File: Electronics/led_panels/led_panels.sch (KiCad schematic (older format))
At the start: 226 parts, among them P5 CONN_2, P6 CONN_2

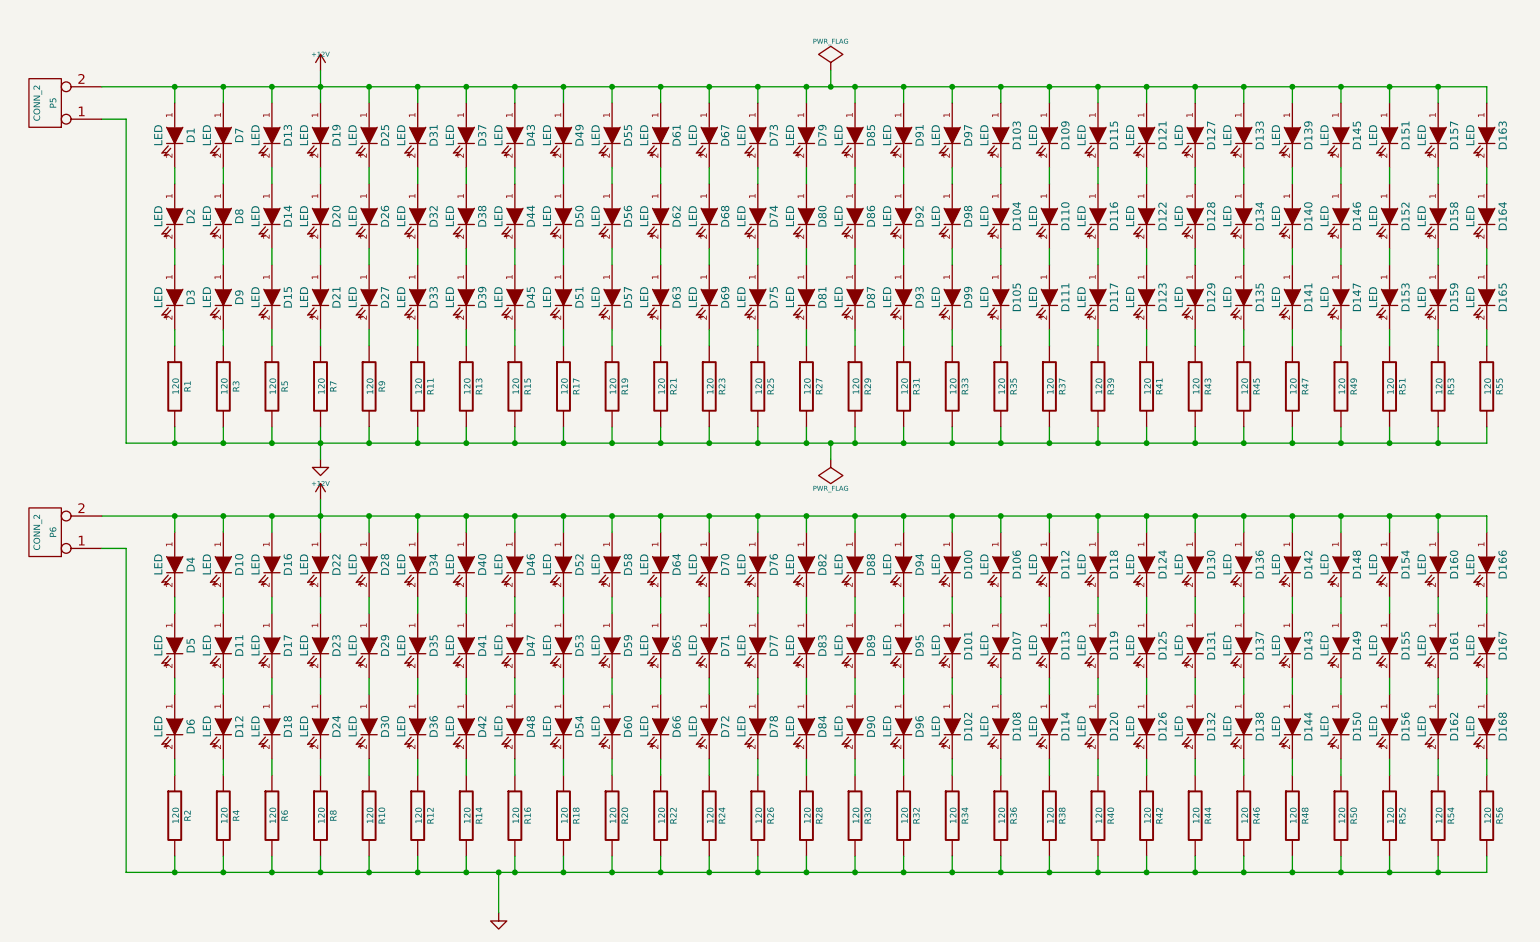
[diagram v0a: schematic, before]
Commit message: Updated board layout. Tidied up schematic.
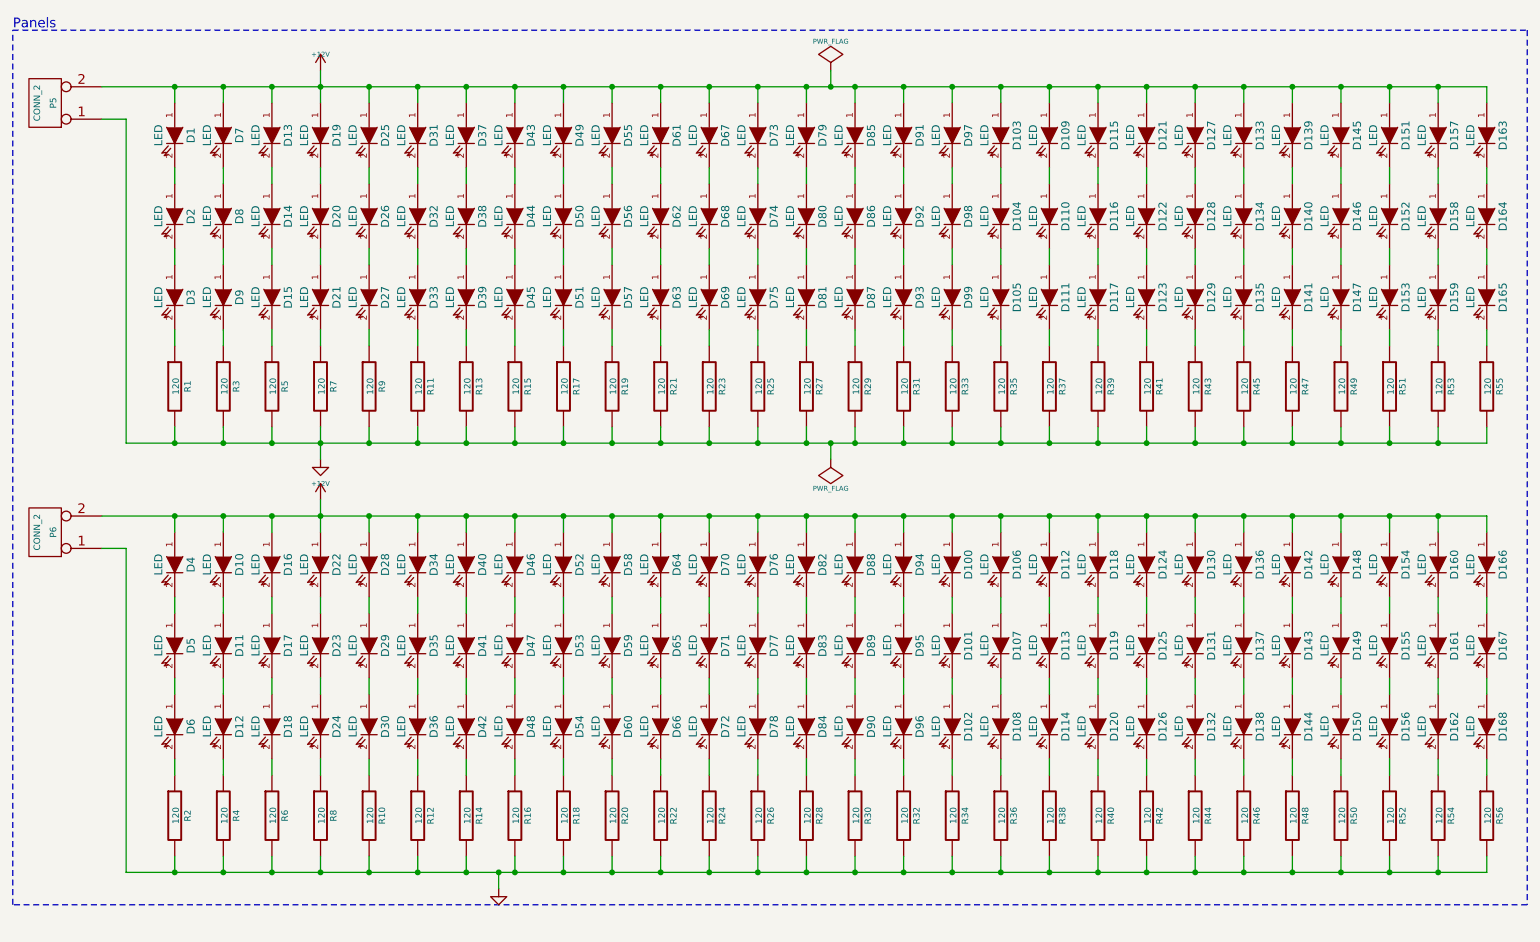
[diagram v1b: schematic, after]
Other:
- note added: "Panels"

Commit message: Tidying.
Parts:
- renumbered P5 to P1, P6 to P2
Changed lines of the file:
@@
 $EndComp
 $Comp
-L CONN_2 P5
+L CONN_2 P1
 U 1 1 5480B6EC
 P 1300 1150
-F 0 "P5" V 1250 1150 40  0000 C CNN
+F 0 "P1" V 1250 1150 40  0000 C CNN
 F 1 "CONN_2" V 1350 1150 40  0000 C CNN
 F 2 "Connect:bornier2" H 1300 1150 60  0001 C CNN
@@
 $EndComp
 $Comp
-L CONN_2 P6
+L CONN_2 P2
 U 1 1 5480BA09
 P 1300 3800
-F 0 "P6" V 1250 3800 40  0000 C CNN
+F 0 "P2" V 1250 3800 40  0000 C CNN
 F 1 "CONN_2" V 1350 3800 40  0000 C CNN
 F 2 "Connect:bornier2" H 1300 3800 60  0001 C CNN

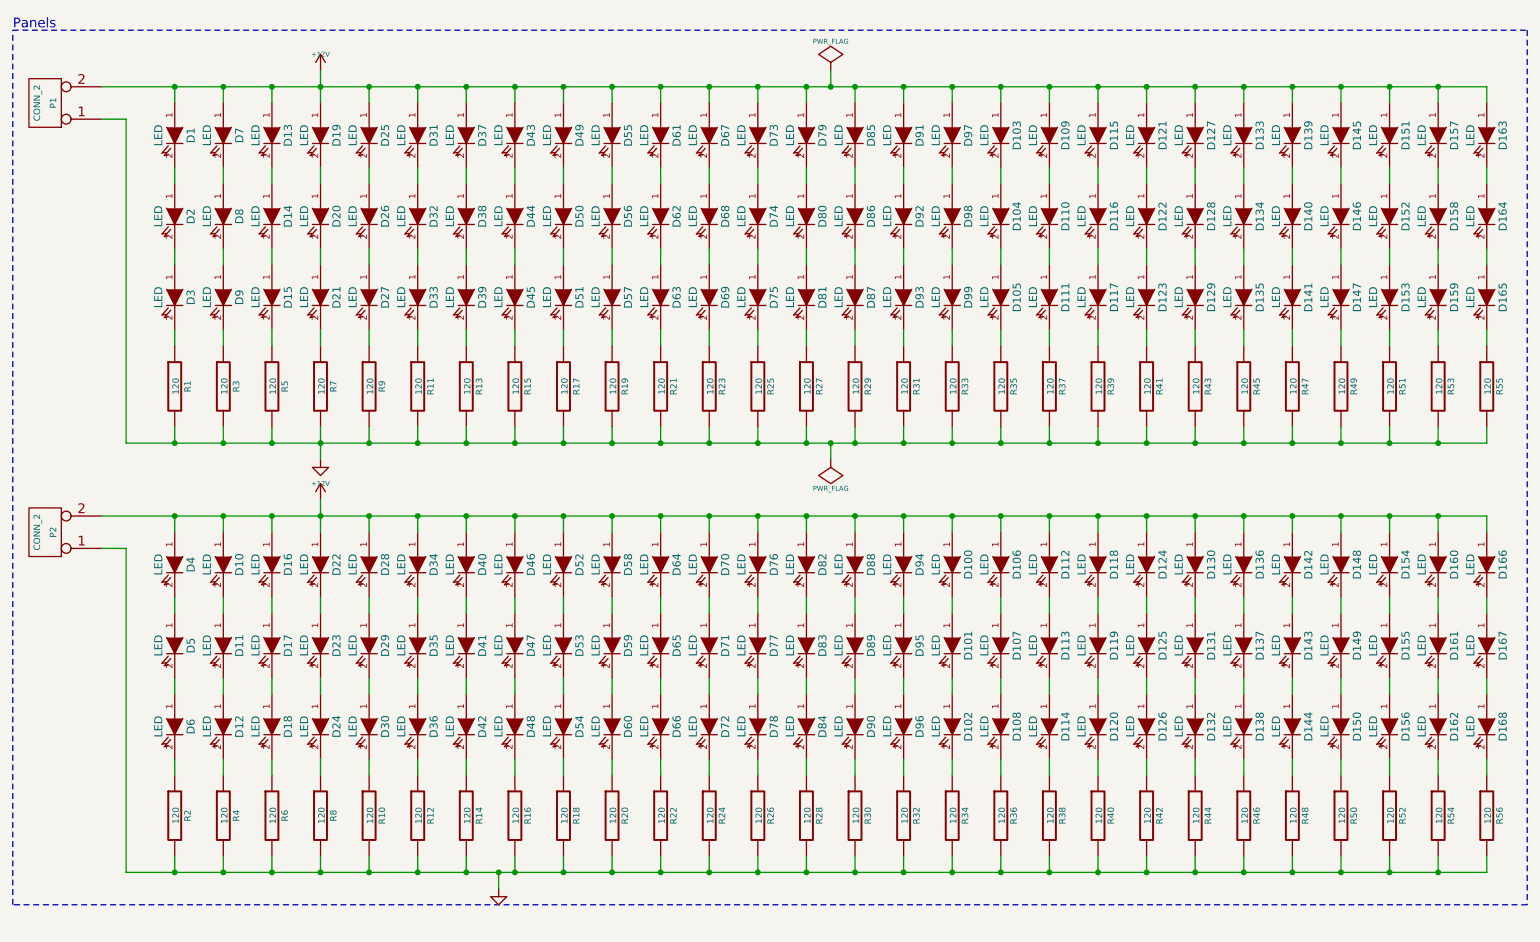
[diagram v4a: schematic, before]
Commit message: Trying out a PCB-based LED panel instead of Veroboard.
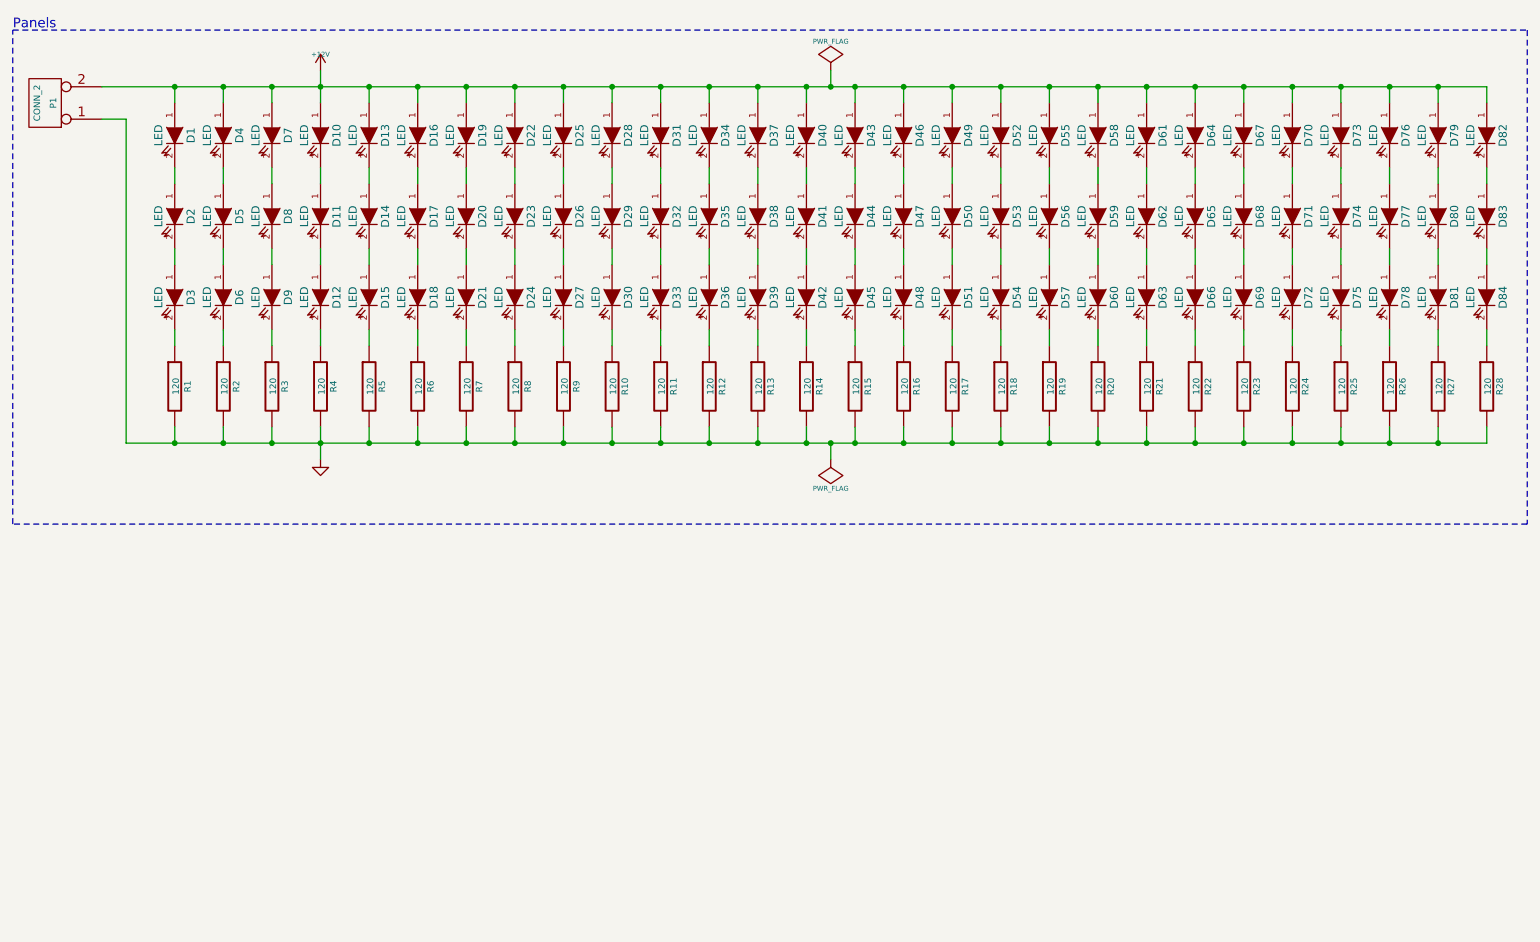
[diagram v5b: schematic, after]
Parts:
- removed D10, D100, D101, D102, D106, D107, D108, D11, D112, D113, D114, D118, D119, D12, D120, D124, D125, D126, D130, D131, D132, D136, D137, D138, D142, D143, D144, D148, D149, D150, D154, D155, D156, D16, D160, D161, D162, D166, D167, D168, D17, D18, D22, D23, D24, D28, D29, D30, D34, D35, D36, D4, D40, D41, D42, D46, D47, D48, D5, D52, D53, D54, D58, D59, D6, D60, D64, D65, D66, D70, D71, D72, D76, D77, D78, D82, D83, D84, D88, D89, D90, D94, D95, D96: LED, LEDs:LED-5MM, symbol LED
- removed P2: CONN_2, Connect:bornier2, symbol CONN_2
- removed R10, R12, R14, R16, R18, R2, R20, R22, R24, R26, R28, R30, R32, R34, R36, R38, R4, R40, R42, R44, R46, R48, R50, R52, R54, R56, R6, R8: 120, Discret:R3, symbol R
- renumbered D19 to D10, D20 to D11, D21 to D12, D25 to D13, D26 to D14, D27 to D15, D31 to D16, D32 to D17, D33 to D18, D37 to D19, D38 to D20, D39 to D21, D43 to D22, D44 to D23, D45 to D24, D49 to D25, D50 to D26, D51 to D27, D55 to D28, D56 to D29, D57 to D30, D61 to D31, D62 to D32, D63 to D33, D67 to D34, D68 to D35, D69 to D36, D73 to D37, D74 to D38, D75 to D39, D7 to D4, D79 to D40, D80 to D41, D81 to D42, D85 to D43, D86 to D44, D87 to D45, D91 to D46, D92 to D47, D93 to D48, D97 to D49, D8 to D5, D98 to D50, D99 to D51, D103 to D52, D104 to D53, D105 to D54, D109 to D55, D110 to D56, D111 to D57, D115 to D58, D116 to D59, D9 to D6, D117 to D60, D121 to D61, D122 to D62, D123 to D63, D127 to D64, D128 to D65, D129 to D66, D133 to D67, D134 to D68, D135 to D69, D13 to D7, D139 to D70, D140 to D71, D141 to D72, D145 to D73, D146 to D74, D147 to D75, D151 to D76, D152 to D77, D153 to D78, D157 to D79, D14 to D8, D158 to D80, D159 to D81, D163 to D82, D164 to D83, D165 to D84, D15 to D9, R19 to R10, R21 to R11, R23 to R12, R25 to R13, R27 to R14, R29 to R15, R31 to R16, R33 to R17, R35 to R18, R37 to R19, R3 to R2, R39 to R20, R41 to R21, R43 to R22, R45 to R23, R47 to R24, R49 to R25, R51 to R26, R53 to R27, R55 to R28, R5 to R3, R7 to R4, R9 to R5, R11 to R6, R13 to R7, R15 to R8, R17 to R9

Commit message: Almost ready for production.
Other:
- note removed: "Panels"
- moved on the sheet: D1, D10, D11, D12, D13, D14, D15, D16, D17, D18, D19, D2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

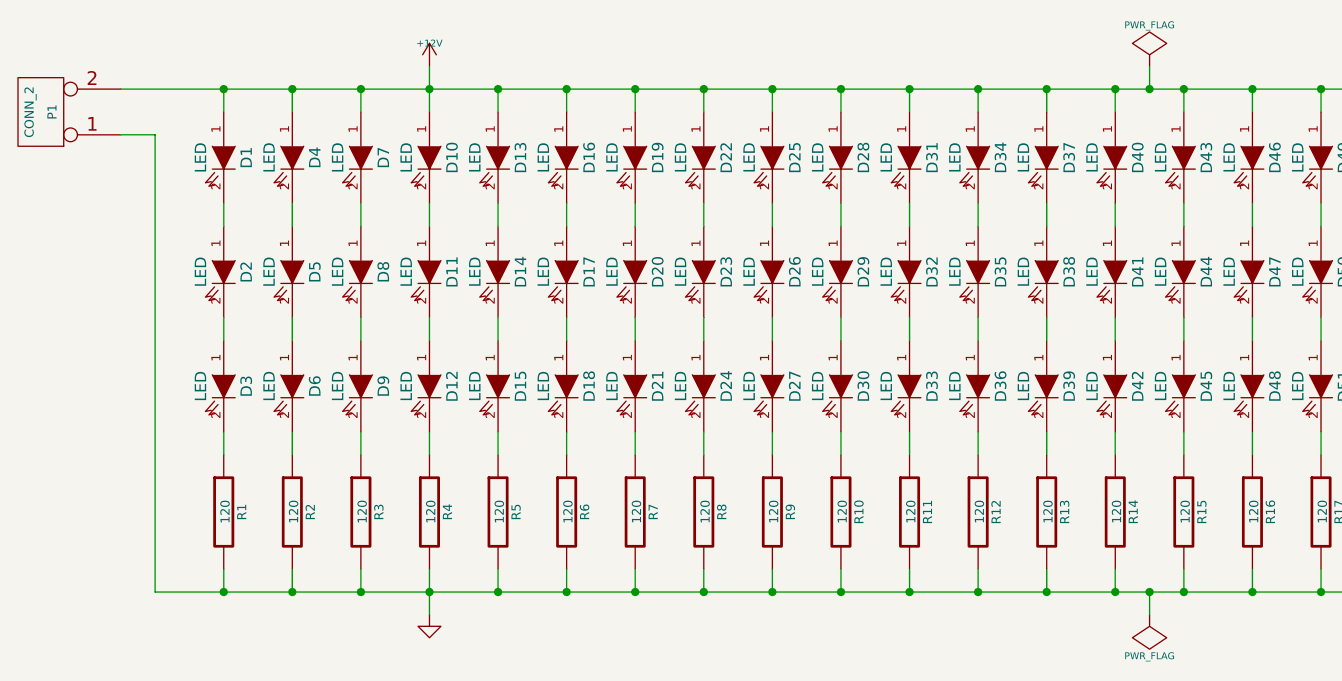
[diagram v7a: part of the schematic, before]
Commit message: Tidied up some visual layout issues.
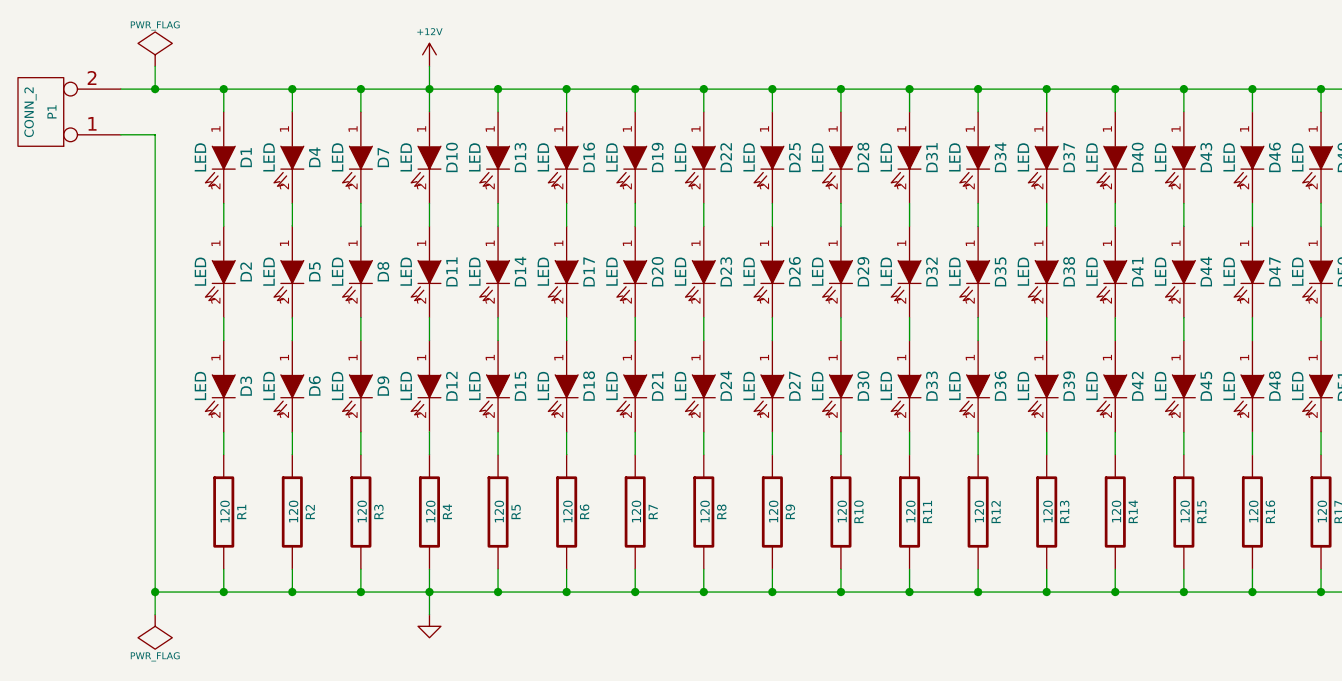
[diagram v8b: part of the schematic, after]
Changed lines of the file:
@@
 EESchema Schematic File Version 2
+LIBS:cylindric
+LIBS:borniers
 LIBS:power
 LIBS:device
@@
 LIBS:contrib
 LIBS:valves
-LIBS:borniers
-LIBS:cylindric
-LIBS:led_panels-cache
 EELAYER 25 0
 EELAYER END
@@
 Sheet 1 1
 Title "UV Exposure Box - LED Panels"
-Date "12 December 2014"
+Date "18 December 2014"
 Rev "1.0"
 Comp ""
@@
 Connection ~ 2100 4750
 Wire Wire Line
-	1800 2750 1800 4750
+	1800 2750 1800 4850
 Connection ~ 2400 4750
 Wire Wire Line
@@
 P 3000 2450
 F 0 "#PWR02" H 3000 2400 20  0001 C CNN
-F 1 "+12V" H 3000 2550 30  0000 C CNN
+F 1 "+12V" H 3000 2600 30  0000 C CNN
 F 2 "" H 3000 2450 60  0000 C CNN
 F 3 "" H 3000 2450 60  0000 C CNN
@@
 L PWR_FLAG #FLG03
 U 1 1 547DC25B
-P 6150 2450
-F 0 "#FLG03" H 6150 2545 30  0001 C CNN
-F 1 "PWR_FLAG" H 6150 2630 30  0000 C CNN
-F 2 "" H 6150 2450 60  0000 C CNN
-F 3 "" H 6150 2450 60  0000 C CNN
-	1    6150 2450
+P 1800 2450
+F 0 "#FLG03" H 1800 2545 30  0001 C CNN
+F 1 "PWR_FLAG" H 1800 2630 30  0000 C CNN
+F 2 "" H 1800 2450 60  0000 C CNN
+F 3 "" H 1800 2450 60  0000 C CNN
+	1    1800 2450
 	1    0    0    -1
 $EndComp
@@
 L PWR_FLAG #FLG04
 U 1 1 547DC26F
-P 6150 4850
-F 0 "#FLG04" H 6150 4945 30  0001 C CNN
-F 1 "PWR_FLAG" H 6150 5030 30  0000 C CNN
-F 2 "" H 6150 4850 60  0000 C CNN
-F 3 "" H 6150 4850 60  0000 C CNN
-	1    6150 4850
+P 1800 4850
+F 0 "#FLG04" H 1800 4945 30  0001 C CNN
+F 1 "PWR_FLAG" H 1800 5030 30  0000 C CNN
+F 2 "" H 1800 4850 60  0000 C CNN
+F 3 "" H 1800 4850 60  0000 C CNN
+	1    1800 4850
 	-1   0    0    1
 $EndComp
-Wire Wire Line
-	6150 4850 6150 4750
-Connection ~ 6150 4750
-Wire Wire Line
-	6150 2450 6150 2550
-Connection ~ 6150 2550
+Connection ~ 1800 4750
+Wire Wire Line
+	1800 2450 1800 2550
+Connection ~ 1800 2550
 $EndSCHEMATC
